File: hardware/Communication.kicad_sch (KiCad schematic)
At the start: 0 parts

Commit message: Populate Current Sensing + Communication sheets; schematic complete
Current Sensing:
- DC-bus shunt (5 mOhm, in series after the eFuse - required renaming
  the eFuse OUT net to +VBUS_EFUSE_OUT so the shunt sits properly
  in-line ahead of +VBUS_PROT)
- INA240 total-bus current sense, unidirectional config, -> MCU ADC

Communication:
- SN65HVD230 CAN transceiver (3.3V native) on ESP32 TWAI pins
- Per-line TVS (SP0115-01UTG) on CANH/CANL
- 4-pin bus connector (CANH/CANL/GND/+VBUS_PROT)

Whole-hierarchy ERC (all 6 sheets + root) now down to 3 residual
errors, all the same benign/expected 'two power_out pins on one net'
pattern (datasheet-recommended parallel pins, or a PWR_FLAG sharing
a net with a real driver) - fully explained in ARCHITECTURE.md, which
now also documents the found-and-worked-around vendor library defects
(eFuse pin-20 duplication, TMP235 VOUT mistyped as input) and confirms
the shunt 'duplicate pins' are correct 4-terminal Kelvin modeling, not
a bug.

All 6 hierarchical sheets are now fully wired end to end:
Power Supply -> MCU Core -> Gate Drive -> Power Stage, with Current
Sensing and Communication cross-wired throughout.

Co-Authored-By: Claude Sonnet 5 <noreply@anthropic.com>
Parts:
- added C34: CAN txcvr decouple, symbol METUPowerLab_Capacitors_Ceramics_SurfaceMounts:100 nF
- added D2: CANH ESD, symbol METUPowerLab_Diodes_TVSDiodes:SP0115-01UTG
- added D3: CANL ESD, symbol METUPowerLab_Diodes_TVSDiodes:SP0115-01UTG
- added J8: CAN_BUS, METUPowerLab_Connectors_SignalConnectors:384471-E, symbol METUPowerLab_Connectors_SignalConnectors:384471-E
- added U10: SN65HVD230DR, METUPowerLab_Interfaces_CANBusBridges:8-SOIC, symbol METUPowerLab_Interfaces_CANBusBridges:SN65HVD230DR
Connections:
- new net +3V3_MCU: C34.1, U10.3 (VCC)
- new net +VBUS_PROT: J8.4
- new net CANH: D2.1, J8.1, U10.7 (CANH)
- new net CANL: D3.1, J8.2, U10.6 (CANL)
- new net CAN_RX: U10.4 (R)
- new net CAN_TX: U10.1 (D)
- new net GND: C34.2, D2.2, D3.2, J8.3, U10.2 (GND), U10.8 (RS)
- no-connect marks 0 -> 2

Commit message: PCB layout: board outline, mounting holes, footprint placement, copper pours, phase-output routing
- 100x115mm 2-layer board, 4x M3 mounting holes, design rules per PowerLab spec
- All 55 schematic components synced to board with real footprints
- Auto-placed via force-directed placement with locked connector/MCU anchors
- GND pour (both layers) + localized pours for VIN_RAW/+VBUS/+VBUS_EFUSE_OUT/+VBUS_PROT/+5V_LOGIC
- Routed the 3 critical phase-output traces (SHA/SHB/SHC, 2mm wide)
- Documented full PCB status in ARCHITECTURE.md: NOT yet fab-ready (732 DRC
  violations, 21 courtyard overlaps, ~50 signal nets still unrouted since
  Freerouting is unavailable in this environment)

Co-Authored-By: Claude Sonnet 5 <noreply@anthropic.com>
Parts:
- C34: footprint (none) -> METUPowerLab_Capacitors_Ceramics_SurfaceMounts:0603_Medium
- D2, D3: footprint (none) -> METUPowerLab_Diodes_TVSDiodes:0603_Small
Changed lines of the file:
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@@
 			)
 		)
-		(property "Footprint" ""
+		(property "Footprint" "METUPowerLab_Capacitors_Ceramics_SurfaceMounts:0603_Medium"
 			(at 65.735 35.56 0)
 			(hide yes)
@@
 			)
 		)
-		(property "Footprint" ""
+		(property "Footprint" "METUPowerLab_Diodes_TVSDiodes:0603_Small"
 			(at 110.49 39.37 0)
 			(hide yes)
@@
 			)
 		)
-		(property "Footprint" ""
+		(property "Footprint" "METUPowerLab_Diodes_TVSDiodes:0603_Small"
 			(at 110.49 54.61 0)
 			(hide yes)

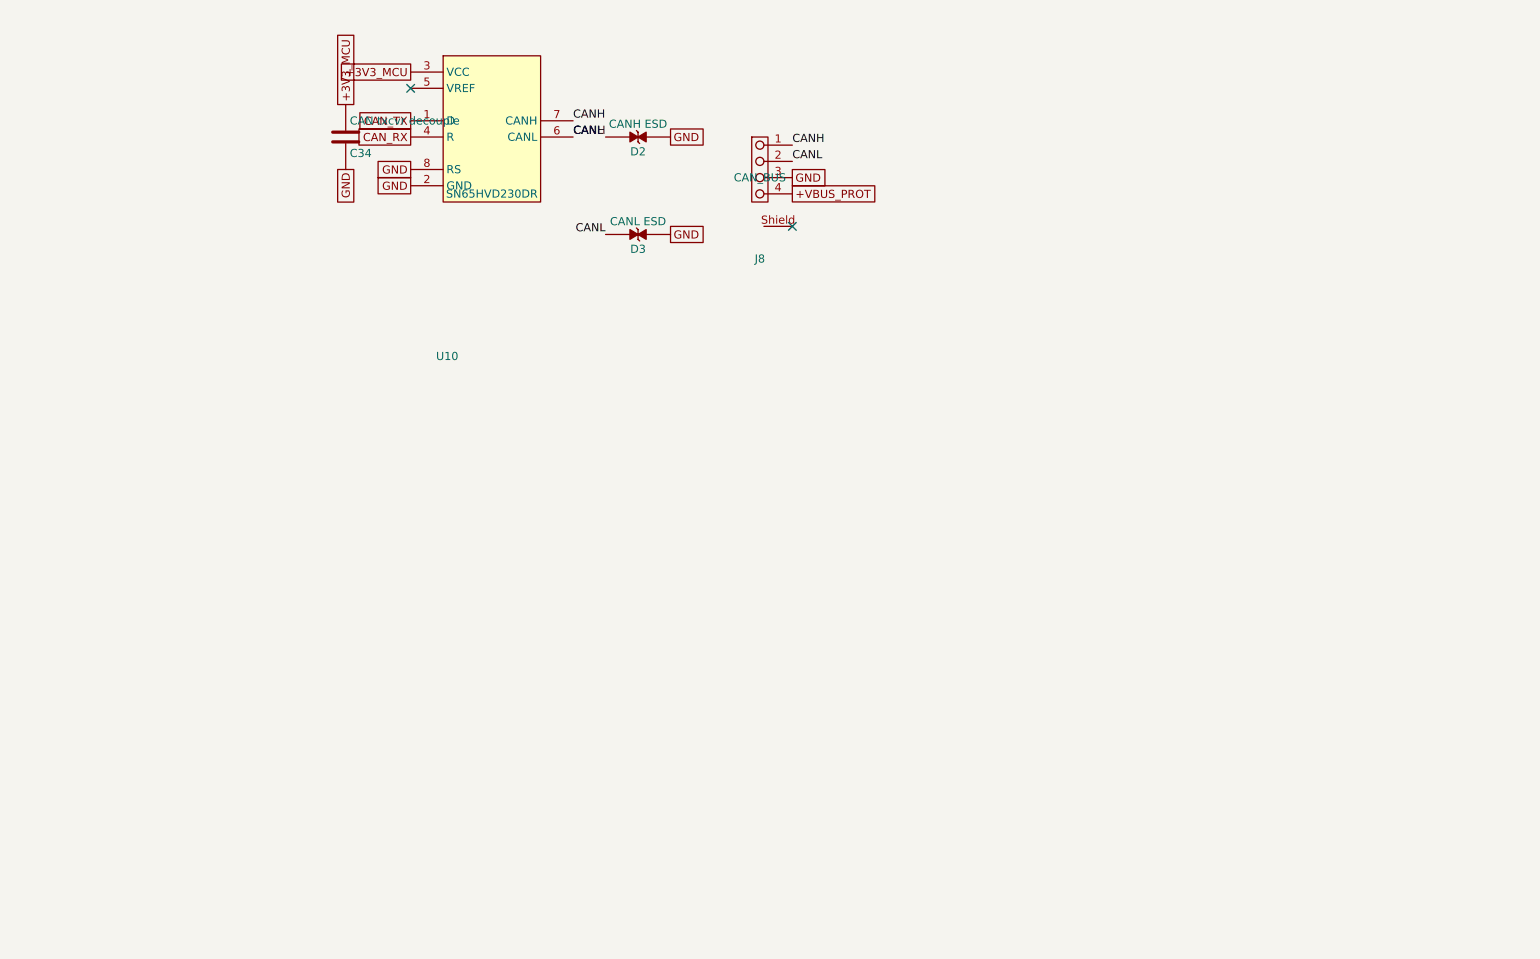
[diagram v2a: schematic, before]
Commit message: Schematic Rev B: full rebuild per METU PowerLab rules
Rev A was withdrawn: labels stuck on pins created real net shorts
(+5V_LOGIC with the 36 V bus, INHA and EFUSE_IMON with GND) and several
circuits contradicted their datasheets.

Rev B: real wires and power symbols on the 2.54 mm grid, hierarchical sheets
(half bridge reused 3x), library values, LAYOUT notes, root page with specs
and block diagram. Circuit fixes: DRV8323 VREF driven, unused buck tied to
GND, INA240A1, LM74700-Q1 reverse polarity, SMBJ36CA, eFuse per datasheet,
direct 3.3 V buck, 4.7 uH/8.1 A inductor, 2512 shunts with net-tie Kelvin,
24 V CAN ESD. kicad-cli ERC: 0 errors; netlist matches intent on all nets.
Old board and project-local library tables removed (board is rebuilt next).

Co-Authored-By: Claude Opus 5.5 <noreply@anthropic.com>
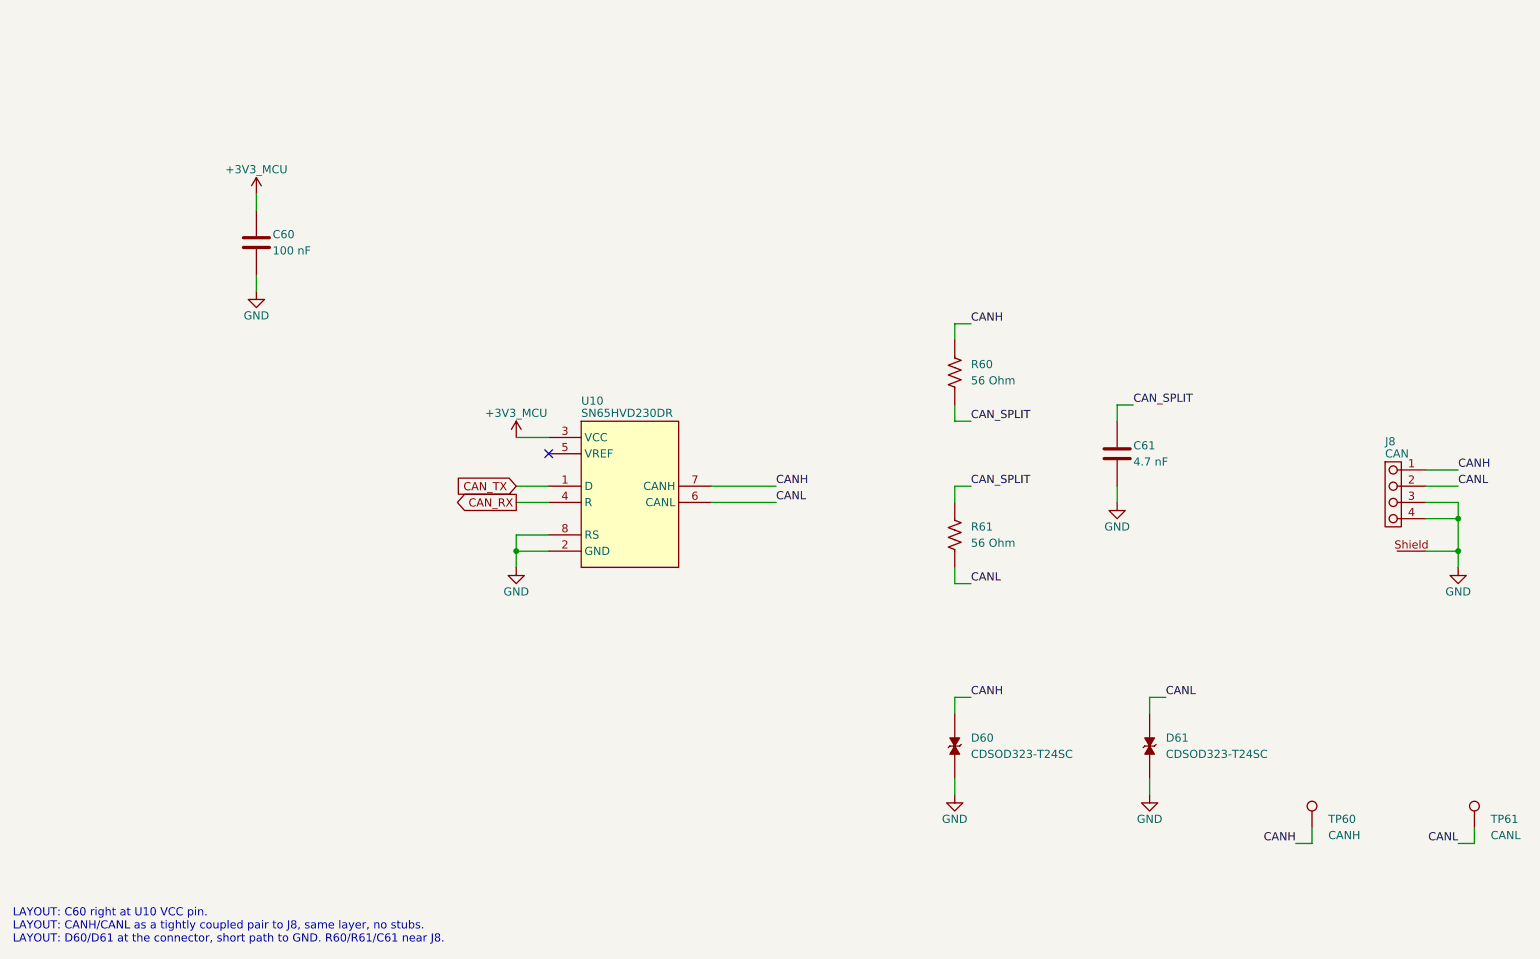
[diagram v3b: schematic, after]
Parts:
- removed C34: CAN txcvr decouple, METUPowerLab_Capacitors_Ceramics_SurfaceMounts:0603_Medium, symbol METUPowerLab_Capacitors_Ceramics_SurfaceMounts:100 nF
- removed D2: CANH ESD, METUPowerLab_Diodes_TVSDiodes:0603_Small, symbol METUPowerLab_Diodes_TVSDiodes:SP0115-01UTG
- removed D3: CANL ESD, METUPowerLab_Diodes_TVSDiodes:0603_Small, symbol METUPowerLab_Diodes_TVSDiodes:SP0115-01UTG
- added C60: 100 nF, METUPowerLab_Capacitors_Ceramics_SurfaceMounts:0603_Medium, symbol METUPowerLab_Capacitors_Ceramics_SurfaceMounts:100 nF
- added C61: 4.7 nF, METUPowerLab_Capacitors_Ceramics_SurfaceMounts:0603_Medium, symbol METUPowerLab_Capacitors_Ceramics_SurfaceMounts:4.7 nF
- added D60, D61: CDSOD323-T24SC, METUPowerLab_Diodes_TVSDiodes:SOD-323, symbol METUPowerLab_Diodes_TVSDiodes:CDSOD323-T24SC
- added R60, R61: 56 Ohm, METUPowerLab_Resistors_ChipResistors:0603_Medium, symbol METUPowerLab_Resistors_ChipResistors:56 Ohm
- added TP60: CANH, METUPowerLab_TestPoints_SurfaceMounts:Pad_D1.5mm, symbol METUPowerLab_TestPoints_SurfaceMounts:TestPoint_Pad
- added TP61: CANL, METUPowerLab_TestPoints_SurfaceMounts:Pad_D1.5mm, symbol METUPowerLab_TestPoints_SurfaceMounts:TestPoint_Pad
- J8: value CAN_BUS -> CAN; Contact Type (none) -> Male Pin; Current Rating (none) -> 12A per Contact; Digi-Key Number (none) -> 2684-384471-ECT-ND; Farnell Number (none) -> 4060713; Manufacturer (none) -> TE Connectivity Erni; Manufacturer Number (none) -> 384471-E; Mounting Type (none) -> Surface Mount, Right Angle; Mouser Number (none) -> 305-384471; Number of Positions (none) -> 4; Number of Rows (none) -> 1; Operating Temperature (none) -> -55°C up to 150°C; Voltage Rating (none) -> -
- U10: Data Rate (none) -> 1Mbps; Digi-Key Number (none) -> 296-11654-1-ND; Duplex (none) -> Half; Farnell Number (none) -> 3124671; Manufacturer (none) -> Texas Instruments; Manufacturer Number (none) -> SN65HVD230DR; Mounting Type (none) -> Surface Mount; Mouser Number (none) -> 595-SN65HVD230DR; Number of Drivers/Receivers (none) -> 1/1; Operating Temperature (none) -> -40°C up to 85°C; Package (none) -> 8-SOIC; Protocol (none) -> CANbus; Receiver Hysteresis (none) -> 100 mV; Voltage Rating (none) -> 3V up to 3.6V; Özdisan Number (none) -> SN65HVD230DR
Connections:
- net +VBUS_PROT is gone; now on net GND: J8.4
- net +3V3_MCU: now also C60.1
- net CANH: now also D60.1, R60.1, TP60.1
- net CANL: now also D61.1, R61.2, TP61.1
- net GND: now also J8.Shield, C60.2, C61.2, D60.2, D61.2
- new net CAN_SPLIT: C61.1, R60.2, R61.1
- no-connect marks 2 -> 1
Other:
- note added: "LAYOUT: C60 right at U10 VCC pin. LAYOUT: CANH/CANL as a tightly coupled pair to J8, same layer, no stubs. LAYOUT: D60/D61 at the connector, short path to GND. R60/R61/C61 near J8."
- title: ${PROJECT_NAME} -> Communication
